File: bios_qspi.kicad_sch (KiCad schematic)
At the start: 4 parts, among them U23 MT25QU01GBBB8_T-PBGA-24

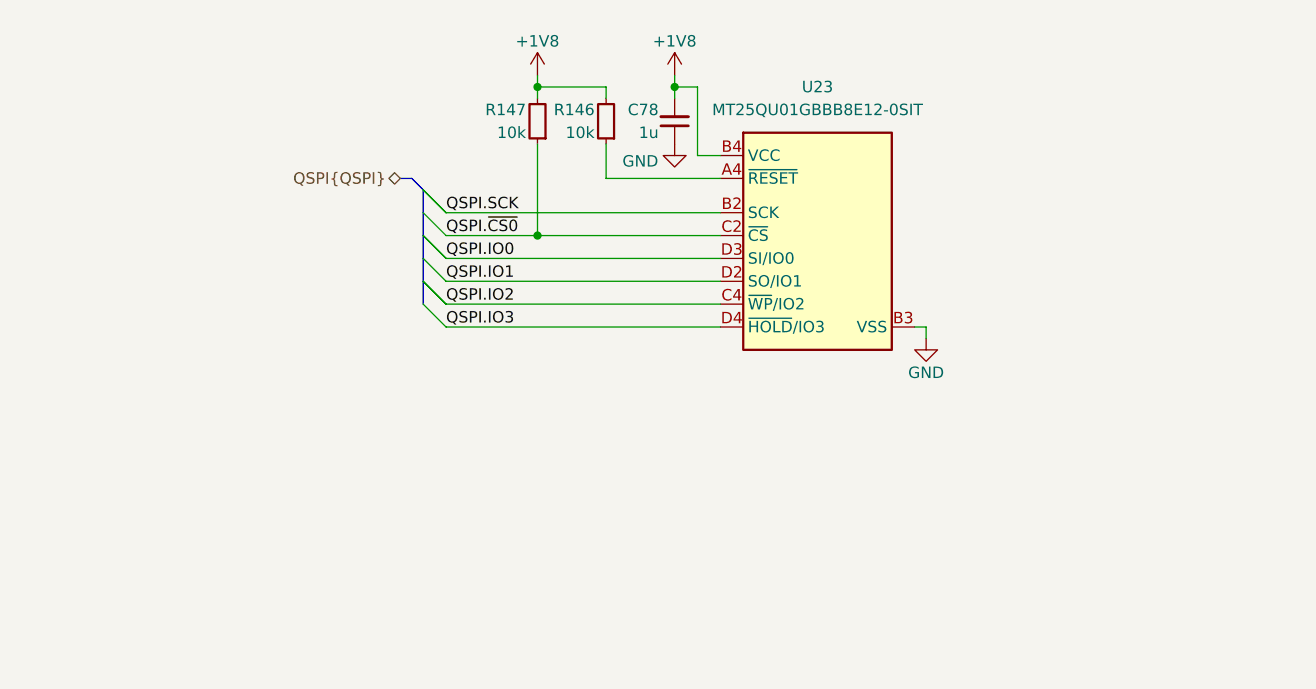
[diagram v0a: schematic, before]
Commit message: [#83652] Add ability to program BIOS SPI flash
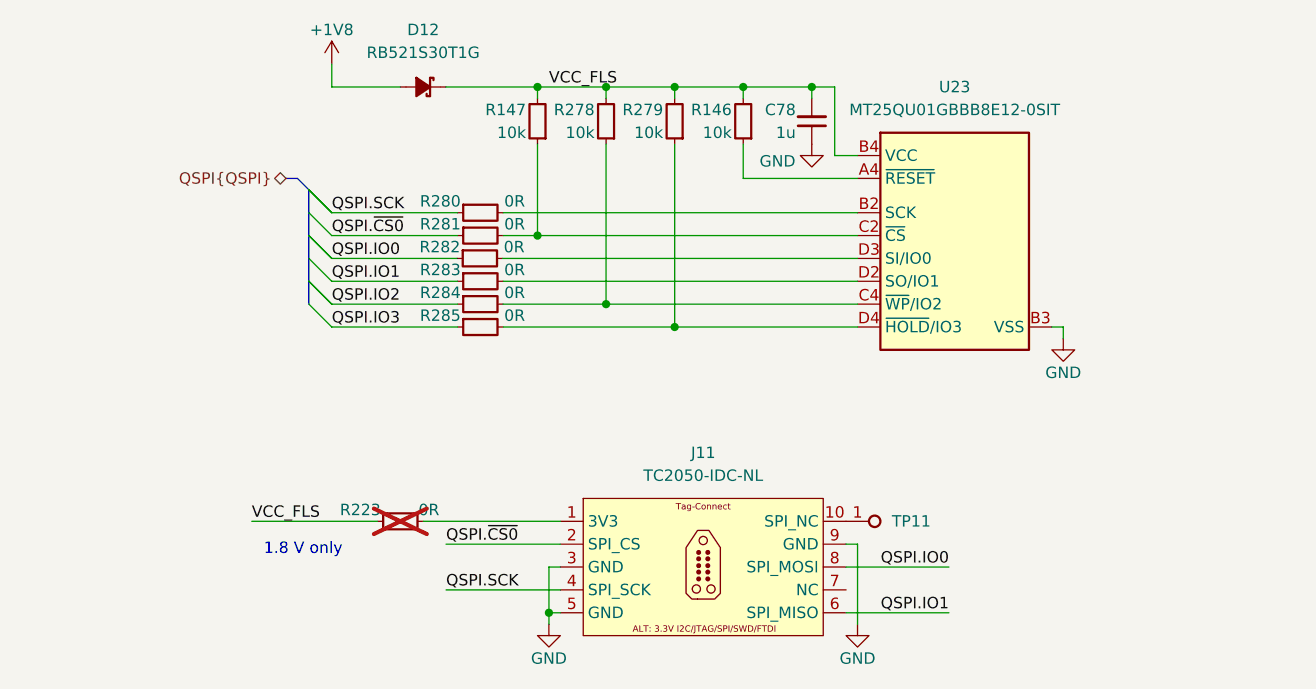
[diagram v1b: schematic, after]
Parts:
- added D12: RB521S30T1G, antmicro-footprints:SOD-523, symbol antmicroDiodesRectifiersSingle:RB521S30T1G
- added J11: Tag-Connect_TC2050-IDC-NL_2x5_P1.27mm, antmicro-footprints:Tag-Connect_TC2050-IDC-NL_2x5_P1.27mm, symbol antmicroTestPoints:Tag-Connect_TC2050-IDC-NL_2x5_P1.27mm
- added R223, R280, R281, R282, R283, R284, R285: R_0R_0402, antmicro-footprints:R_0402_1005Metric, symbol antmicroResistors0402:R_0R_0402
- added R278, R279: R_10k_0402, antmicro-footprints:R_0402_1005Metric, symbol antmicroResistors0402:R_10k_0402
- added TP11: TP_0.75mm_SMD, antmicro-footprints:TP_SMD_0.75mm, symbol antmicroTestPoints:TP_0.75mm_SMD
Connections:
- net +1V8: now also D12.2 (A); no longer C78.2, R146.2, R147.2, U23.B4 (VCC)
- net GND: now also J11.3, J11.5, J11.9
- net QSPI.IO0: now also J11.8, R282.1; no longer U23.D3 (SI/IO0)
- net QSPI.IO1: now also J11.6, R283.1; no longer U23.D2 (SO/IO1)
- net QSPI.IO2: now also R284.1; no longer U23.C4 (~{WP}/IO2)
- net QSPI.IO3: now also R285.1; no longer U23.D4 (~{HOLD}/IO3)
- net QSPI.SCK: now also J11.4, R280.1; no longer U23.B2 (SCK)
- net QSPI.~{CS0}: now also J11.2, R281.1; no longer R147.1, U23.C2 (~{CS})
- new net: R147.1, R281.2, U23.C2 (~{CS})
- new net: R279.1, R285.2, U23.D4 (~{HOLD}/IO3)
- new net: R280.2, U23.B2 (SCK)
- new net: R283.2, U23.D2 (SO/IO1)
- new net: J11.1, R223.2
- new net: R278.1, R284.2, U23.C4 (~{WP}/IO2)
- new net: R282.2, U23.D3 (SI/IO0)
- new net: J11.10, TP11.1
- new net VCC_FLS: C78.2, D12.1 (C), R146.2, R147.2, R223.1, R278.2, R279.2, U23.B4 (VCC)
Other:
- note added: "1.8 V only"
- moved on the sheet: C78, R146, U23

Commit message: [#83609] Reannotate board
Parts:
- renumbered C78 to C161, D12 to D19, R223 to R272, R282 to R273, R280 to R274, R281 to R275, R283 to R276, R284 to R277, R285 to R278, R147 to R279, R278 to R280, R279 to R281, R146 to R282, TP11 to TP23, U23 to U32
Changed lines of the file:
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@@
 		(on_board yes)
 		(dnp no)
-		(property "Reference" "R281"
+		(property "Reference" "R275"
 			(at 187.325 144.78 0)
 			(effects
@@
 			(project "bmc-reference-carrier-board"
 				(path "/5f636c45-3c15-4731-8931-4625e0dab7e4/f7dd1d4e-8165-4fe2-a0a6-b4960a02bfaf"
-					(reference "R281")
+					(reference "R275")
 					(unit 1)
 				)
@@
 		(on_board yes)
 		(dnp no)
-		(property "Reference" "D12"
+		(property "Reference" "D19"
 			(at 185.42 123.19 0)
 			(effects
@@
 			(project "bmc-reference-carrier-board"
 				(path "/5f636c45-3c15-4731-8931-4625e0dab7e4/f7dd1d4e-8165-4fe2-a0a6-b4960a02bfaf"
-					(reference "D12")
+					(reference "D19")
 					(unit 1)
 				)
@@
 		(on_board yes)
 		(dnp no)
-		(property "Reference" "R285"
+		(property "Reference" "R278"
 			(at 187.325 154.94 0)
 			(effects
@@
 			(project "bmc-reference-carrier-board"
 				(path "/5f636c45-3c15-4731-8931-4625e0dab7e4/f7dd1d4e-8165-4fe2-a0a6-b4960a02bfaf"
-					(reference "R285")
+					(reference "R278")
 					(unit 1)
 				)
@@
 		(on_board yes)
 		(dnp no)
-		(property "Reference" "R280"
+		(property "Reference" "R274"
 			(at 187.325 142.24 0)
 			(effects
@@
 			(project ""
 				(path "/5f636c45-3c15-4731-8931-4625e0dab7e4/f7dd1d4e-8165-4fe2-a0a6-b4960a02bfaf"
-					(reference "R280")
+					(reference "R274")
 					(unit 1)
 				)
@@
 		(on_board yes)
 		(dnp no)
-		(property "Reference" "#PWR0268"
+		(property "Reference" "#PWR0309"
 			(at 208.28 191.77 0)
 			(effects
@@
 			(project "bmc-reference-carrier-board"
 				(path "/5f636c45-3c15-4731-8931-4625e0dab7e4/f7dd1d4e-8165-4fe2-a0a6-b4960a02bfaf"
-					(reference "#PWR0268")
+					(reference "#PWR0309")
 					(unit 1)
 				)
@@
 		(on_board yes)
 		(dnp no)
-		(property "Reference" "#PWR0140"
+		(property "Reference" "#PWR0310"
 			(at 219.71 138.43 0)
 			(effects
@@
 			(project "bmc-reference-carrier-board"
 				(path "/5f636c45-3c15-4731-8931-4625e0dab7e4/f7dd1d4e-8165-4fe2-a0a6-b4960a02bfaf"
-					(reference "#PWR0140")
+					(reference "#PWR0310")
 					(unit 1)
 				)
@@
 		(on_board yes)
 		(dnp no)
-		(property "Reference" "R283"
+		(property "Reference" "R276"
 			(at 187.325 149.86 0)
 			(effects
@@
 			(project "bmc-reference-carrier-board"
 				(path "/5f636c45-3c15-4731-8931-4625e0dab7e4/f7dd1d4e-8165-4fe2-a0a6-b4960a02bfaf"
-					(reference "R283")
+					(reference "R276")
 					(unit 1)
 				)
@@
 		(on_board yes)
 		(dnp yes)
-		(property "Reference" "R223"
+		(property "Reference" "R272"
 			(at 178.435 176.53 0)
 			(effects
@@
 			(project "bmc-reference-carrier-board"
 				(path "/5f636c45-3c15-4731-8931-4625e0dab7e4/f7dd1d4e-8165-4fe2-a0a6-b4960a02bfaf"
-					(reference "R223")
+					(reference "R272")
 					(unit 1)
 				)
@@
 		(on_board yes)
 		(dnp no)
-		(property "Reference" "R278"
+		(property "Reference" "R280"
 			(at 204.47 132.08 90)
 			(effects
@@
 			(project "bmc-reference-carrier-board"
 				(path "/5f636c45-3c15-4731-8931-4625e0dab7e4/f7dd1d4e-8165-4fe2-a0a6-b4960a02bfaf"
-					(reference "R278")
+					(reference "R280")
 					(unit 1)
 				)
@@
 		(on_board yes)
 		(dnp no)
-		(property "Reference" "R146"
+		(property "Reference" "R282"
 			(at 219.71 132.08 90)
 			(effects
@@
 			(project "bmc-reference-carrier-board"
 				(path "/5f636c45-3c15-4731-8931-4625e0dab7e4/f7dd1d4e-8165-4fe2-a0a6-b4960a02bfaf"
-					(reference "R146")
+					(reference "R282")
 					(unit 1)
 				)
@@
 		(on_board yes)
 		(dnp no)
-		(property "Reference" "R279"
+		(property "Reference" "R281"
 			(at 212.09 132.08 90)
 			(effects
@@
 			(project "bmc-reference-carrier-board"
 				(path "/5f636c45-3c15-4731-8931-4625e0dab7e4/f7dd1d4e-8165-4fe2-a0a6-b4960a02bfaf"
-					(reference "R279")
+					(reference "R281")
 					(unit 1)
 				)
@@
 		(on_board yes)
 		(dnp no)
-		(property "Reference" "#PWR0141"
+		(property "Reference" "#PWR0308"
 			(at 160.02 129.54 0)
 			(effects
@@
 			(project "bmc-reference-carrier-board"
 				(path "/5f636c45-3c15-4731-8931-4625e0dab7e4/f7dd1d4e-8165-4fe2-a0a6-b4960a02bfaf"
-					(reference "#PWR0141")
+					(reference "#PWR0308")
 					(unit 1)
 				)
@@
 		(on_board yes)
 		(dnp no)
-		(property "Reference" "#PWR0138"
+		(property "Reference" "#PWR0312"
 			(at 247.65 160.02 0)
 			(effects
@@
 			(project "bmc-reference-carrier-board"
 				(path "/5f636c45-3c15-4731-8931-4625e0dab7e4/f7dd1d4e-8165-4fe2-a0a6-b4960a02bfaf"
-					(reference "#PWR0138")
+					(reference "#PWR0312")
 					(unit 1)
 				)
@@
 		(on_board yes)
 		(dnp no)
-		(property "Reference" "R282"
+		(property "Reference" "R273"
 			(at 187.2714 147.32 0)
 			(effects
@@
 			(project "bmc-reference-carrier-board"
 				(path "/5f636c45-3c15-4731-8931-4625e0dab7e4/f7dd1d4e-8165-4fe2-a0a6-b4960a02bfaf"
-					(reference "R282")
+					(reference "R273")
 					(unit 1)
 				)
@@
 		(dnp no)
 		(fields_autoplaced yes)
-		(property "Reference" "U23"
+		(property "Reference" "U32"
 			(at 244.475 129.54 0)
 			(effects
@@
 			(project "bmc-reference-carrier-board"
 				(path "/5f636c45-3c15-4731-8931-4625e0dab7e4/f7dd1d4e-8165-4fe2-a0a6-b4960a02bfaf"
-					(reference "U23")
+					(reference "U32")
 					(unit 1)
 				)
@@
 		(on_board yes)
 		(dnp no)
-		(property "Reference" "#PWR0269"
+		(property "Reference" "#PWR0311"
 			(at 242.57 191.77 0)
 			(effects
@@
 			(project "bmc-reference-carrier-board"
 				(path "/5f636c45-3c15-4731-8931-4625e0dab7e4/f7dd1d4e-8165-4fe2-a0a6-b4960a02bfaf"
-					(reference "#PWR0269")
+					(reference "#PWR0311")
 					(unit 1)
 				)
@@
 		(dnp no)
 		(fields_autoplaced yes)
-		(property "Reference" "TP11"
+		(property "Reference" "TP23"
 			(at 237.49 177.8 0)
 			(effects
@@
 			(project "bmc-reference-carrier-board"
 				(path "/5f636c45-3c15-4731-8931-4625e0dab7e4/f7dd1d4e-8165-4fe2-a0a6-b4960a02bfaf"
-					(reference "TP11")
+					(reference "TP23")
 					(unit 1)
 				)
@@
 		(on_board yes)
 		(dnp no)
-		(property "Reference" "R147"
+		(property "Reference" "R279"
 			(at 196.85 132.08 90)
 			(effects
@@
 			(project "bmc-reference-carrier-board"
 				(path "/5f636c45-3c15-4731-8931-4625e0dab7e4/f7dd1d4e-8165-4fe2-a0a6-b4960a02bfaf"
-					(reference "R147")
+					(reference "R279")
 					(unit 1)
 				)
@@
 		(on_board yes)
 		(dnp no)
-		(property "Reference" "R284"
+		(property "Reference" "R277"
 			(at 187.325 152.4 0)
 			(effects
@@
 			(project "bmc-reference-carrier-board"
 				(path "/5f636c45-3c15-4731-8931-4625e0dab7e4/f7dd1d4e-8165-4fe2-a0a6-b4960a02bfaf"
-					(reference "R284")
+					(reference "R277")
 					(unit 1)
 				)
@@
 		(on_board yes)
 		(dnp no)
-		(property "Reference" "C78"
+		(property "Reference" "C161"
 			(at 226.822 132.08 90)
 			(effects
@@
 			(project "bmc-reference-carrier-board"
 				(path "/5f636c45-3c15-4731-8931-4625e0dab7e4/f7dd1d4e-8165-4fe2-a0a6-b4960a02bfaf"
-					(reference "C78")
+					(reference "C161")
 					(unit 1)
 				)

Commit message: [#83736] WIP: Clear ERC
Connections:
- no-connect marks 0 -> 1
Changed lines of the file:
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@@
+	)
+	(junction
+		(at 231.14 129.54)
+		(diameter 0)
+		(color 0 0 0 0)
 	)
 	(junction
@@
 		(color 0 0 0 0)
 	)
+	(no_connect
+		(at 232.41 185.42)
+	)
 	(bus_entry
 		(at 172.72 151.13)
@@
 	(wire
 		(pts
-			(xy 189.1764 148.59) (xy 175.26 148.59)
+			(xy 189.23 148.59) (xy 175.26 148.59)
 		)
 		(stroke
@@
 		)
 	)
+	(wire
+		(pts
+			(xy 231.14 128.27) (xy 231.14 129.54)
+		)
+		(stroke
+			(width 0)
+			(type default)
+		)
+	)
 	(bus
 		(pts
@@
 	(wire
 		(pts
-			(xy 233.68 148.59) (xy 194.2564 148.59)
+			(xy 233.68 148.59) (xy 194.31 148.59)
 		)
 		(stroke
@@
 	)
 	(symbol
+		(lib_id "antmicropower:PWR_FLAG")
+		(at 231.14 128.27 0)
+		(unit 1)
+		(exclude_from_sim no)
+		(in_bom yes)
+		(on_board yes)
+		(dnp no)
+		(fields_autoplaced yes)
+		(property "Reference" "#FLG08"
+			(at 231.14 126.365 0)
+			(effects
+				(font
+					(size 1.27 1.27)
+				)
+				(hide yes)
+			)
+		)
+		(property "Value" "PWR_FLAG"
+			(at 231.14 123.19 0)
+			(effects
+				(font
+					(size 1.27 1.27)
+				)
+			)
+		)
+		(property "Footprint" ""
+			(at 231.14 128.27 0)
+			(effects
+				(font
+					(size 1.27 1.27)
+				)
+				(hide yes)
+			)
+		)
+		(property "Datasheet" ""
+			(at 231.14 128.27 0)
+			(effects
+				(font
+					(size 1.27 1.27)
+				)
+				(hide yes)
+			)
+		)
+		(property "Description" ""
+			(at 231.14 128.27 0)
+			(effects
+				(font
+					(size 1.27 1.27)
+				)
+				(hide yes)
+			)
+		)
+		(pin "1"
+		)
+		(instances
+			(project ""
+				(path "/5f636c45-3c15-4731-8931-4625e0dab7e4/f7dd1d4e-8165-4fe2-a0a6-b4960a02bfaf"
+					(reference "#FLG08")
+					(unit 1)
+				)
+			)
+		)
+	)
+	(symbol
 		(lib_id "antmicroResistors0402:R_0R_0402")
 		(at 180.34 177.8 0)
@@
 	(symbol
 		(lib_id "antmicroResistors0402:R_0R_0402")
-		(at 189.1764 148.59 0)
+		(at 189.23 148.59 0)
 		(unit 1)
 		(exclude_from_sim no)
@@
 		(dnp no)
 		(property "Reference" "R273"
-			(at 187.2714 147.32 0)
+			(at 187.325 147.32 0)
 			(effects
 				(font
@@
 		)
 		(property "Value" "R_0R_0402"
-			(at 209.4964 161.29 0)
+			(at 209.55 161.29 0)
 			(effects
 				(font
@@
 		)
 		(property "Footprint" "antmicro-footprints:R_0402_1005Metric"
-			(at 209.4964 163.83 0)
+			(at 209.55 163.83 0)
 			(effects
 				(font
@@
 		)
 		(property "Datasheet" "https://industrial.panasonic.com/cdbs/www-data/pdf/RDA0000/AOA0000C301.pdf"
-			(at 209.4964 166.37 0)
+			(at 209.55 166.37 0)
 			(effects
 				(font
@@
 		)
 		(property "Description" "SMD Chip Resistor, Jumper, 0 ohm, 100 mW, 0402 [1005 Metric], Thick Film, General Purpose"
-			(at 189.1764 148.59 0)
+			(at 189.23 148.59 0)
 			(effects
 				(font
@@
 		)
 		(property "MPN" "ERJ2GE0R00X"
-			(at 209.4964 168.91 0)
+			(at 209.55 168.91 0)
 			(effects
 				(font
@@
 		)
 		(property "Manufacturer" "Panasonic"
-			(at 209.4964 171.45 0)
+			(at 209.55 171.45 0)
 			(effects
 				(font
@@
 		)
 		(property "License" "Apache-2.0"
-			(at 209.4964 173.99 0)
+			(at 209.55 173.99 0)
 			(effects
 				(font
@@
 		)
 		(property "Author" "Antmicro"
-			(at 209.4964 176.53 0)
+			(at 209.55 176.53 0)
 			(effects
 				(font
@@
 		)
 		(property "Val" "0R"
-			(at 195.5264 147.32 0)
+			(at 195.58 147.32 0)
 			(effects
 				(font
@@
 		)
 		(property "Tolerance" "~"
-			(at 209.4964 158.75 0)
+			(at 209.55 158.75 0)
 			(effects
 				(font
@@
 		)
 		(property "Current" "1A"
-			(at 209.4964 179.07 0)
-			(effects
-				(font
+			(at 209.55 179.07 0)
+			(effects
+				(font

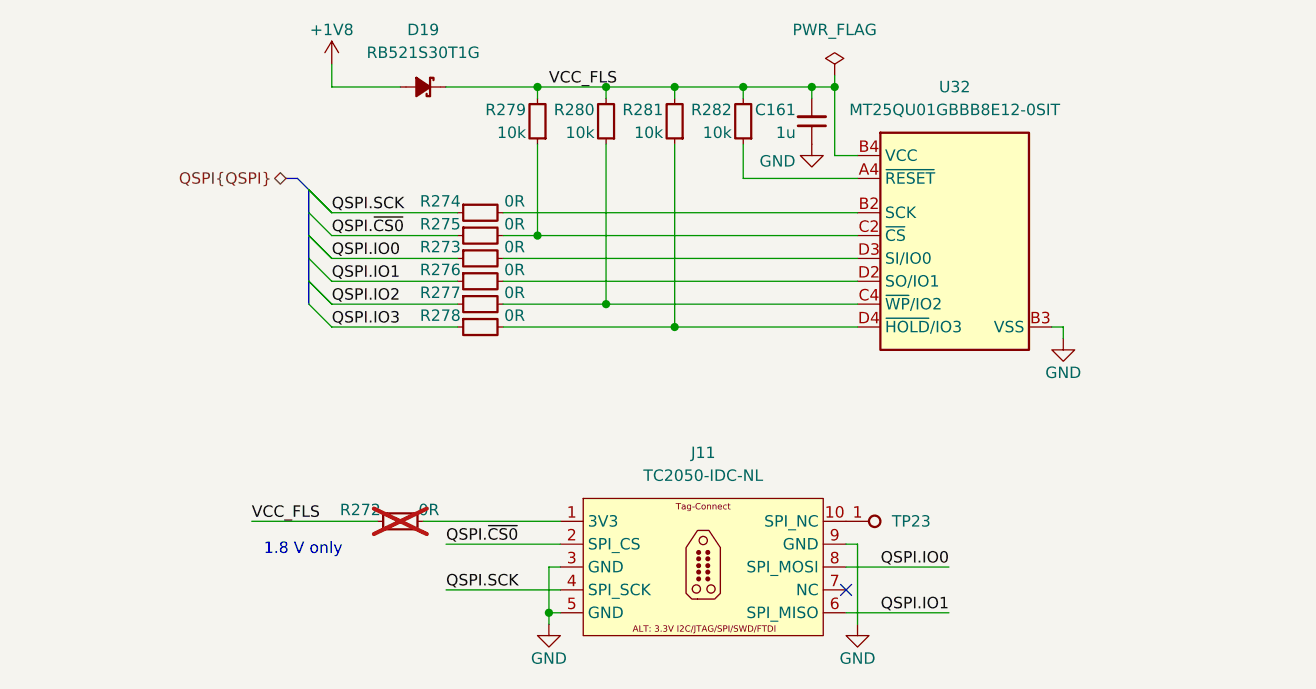
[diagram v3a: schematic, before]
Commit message: [#83767] Connect J11 to U32 without R0
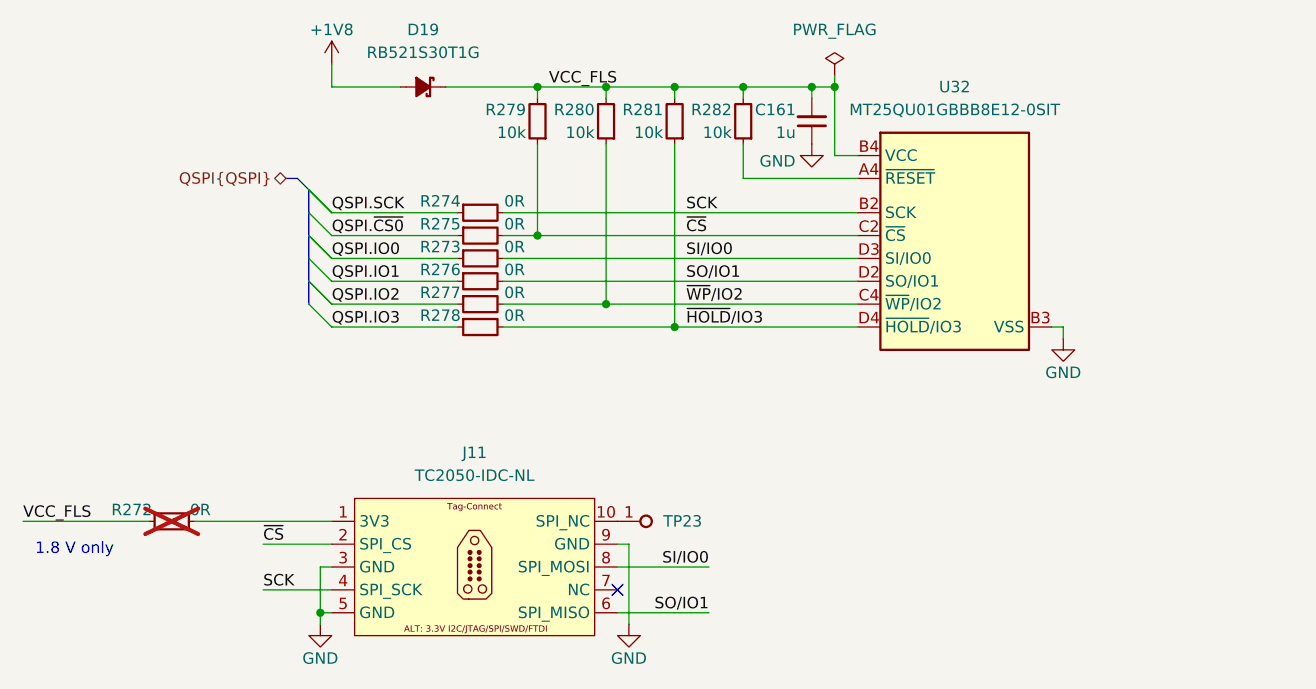
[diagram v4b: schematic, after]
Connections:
- net QSPI.IO0: no longer J11.8
- net QSPI.IO1: no longer J11.6
- net QSPI.SCK: no longer J11.4
- net QSPI.~{CS0}: no longer J11.2
- net ~{CS}: now reaches R275.2, R279.1, U32.C2 (~{CS})
- net ~{CS}: now also J11.2
- net ~{HOLD}/IO3: now reaches R278.2, R281.1, U32.D4 (~{HOLD}/IO3)
- net SCK: now reaches R274.2, U32.B2 (SCK)
- net SCK: now also J11.4
- net SO/IO1: now reaches R276.2, U32.D2 (SO/IO1)
- net SO/IO1: now also J11.6
- net ~{WP}/IO2: now reaches R277.2, R280.1, U32.C4 (~{WP}/IO2)
- net SI/IO0: now reaches R273.2, U32.D3 (SI/IO0)
- net SI/IO0: now also J11.8
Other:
- moved on the sheet: J11, R272, TP23

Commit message: [#83767] Replace BIOS flash with SO-16 package
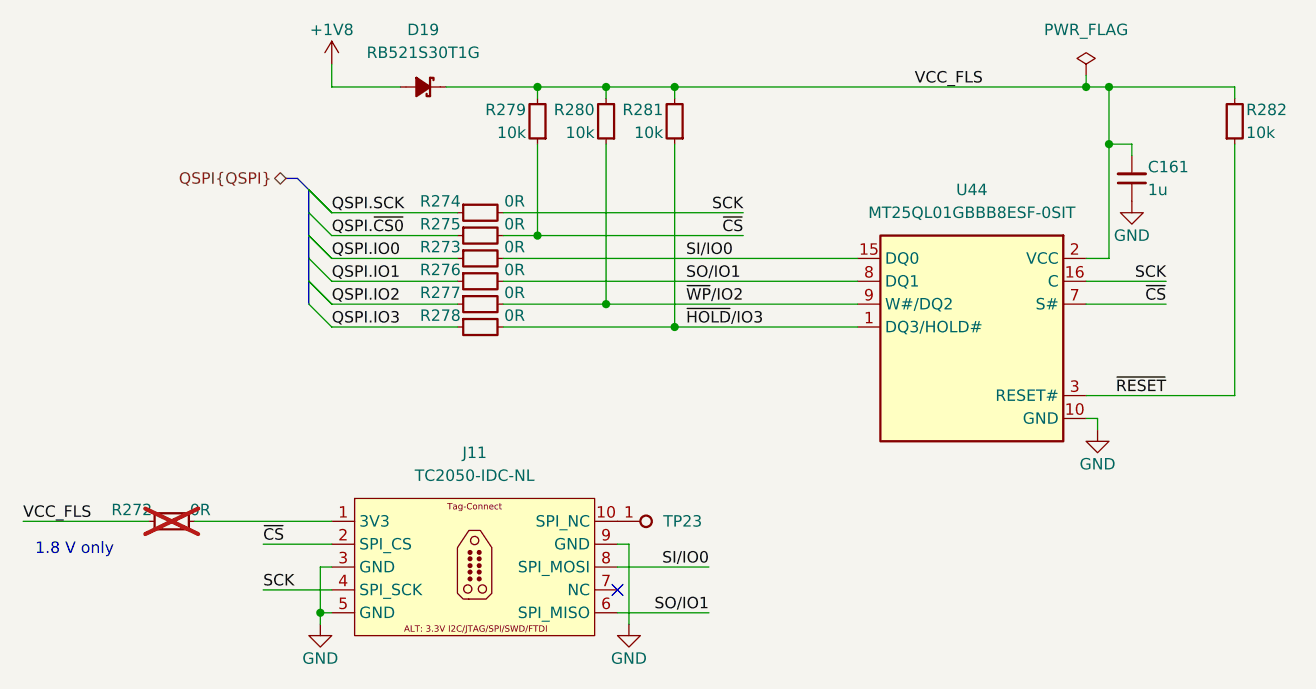
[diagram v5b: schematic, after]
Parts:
- removed U32: MT25QU01GBBB8_T-PBGA-24, antmicro-footprints:BGA-25-24_6x8mm_Layout5x5_P1x1mm, symbol antmicroMemory:MT25QU01GBBB8_T-PBGA-24
- added U44: MT25QL01GBBB8E_SOP2-16, antmicro-footprints:SOP2-16_7.5x10.3mm, symbol antmicroMemory:MT25QL01GBBB8E_SOP2-16
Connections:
- net GND: now also U44.10 (GND)
- net SCK: now also U44.16 (C)
- net SI/IO0: now also U44.15 (DQ0)
- net SO/IO1: now also U44.8 (DQ1)
- net VCC_FLS: now also U44.2 (VCC)
- net ~{CS}: now also U44.7 (S#)
- net ~{HOLD}/IO3: now also U44.1 (DQ3/HOLD#)
- net ~{WP}/IO2: now also U44.9 (W#/DQ2)
- net ~{RESET}: now reaches R282.1
- net ~{RESET}: now also U44.3 (RESET#)
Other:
- moved on the sheet: C161, R282
